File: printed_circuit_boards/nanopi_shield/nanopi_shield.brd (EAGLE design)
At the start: 48.2 x 42.9 mm, 4 parts, among them X1 1365-40

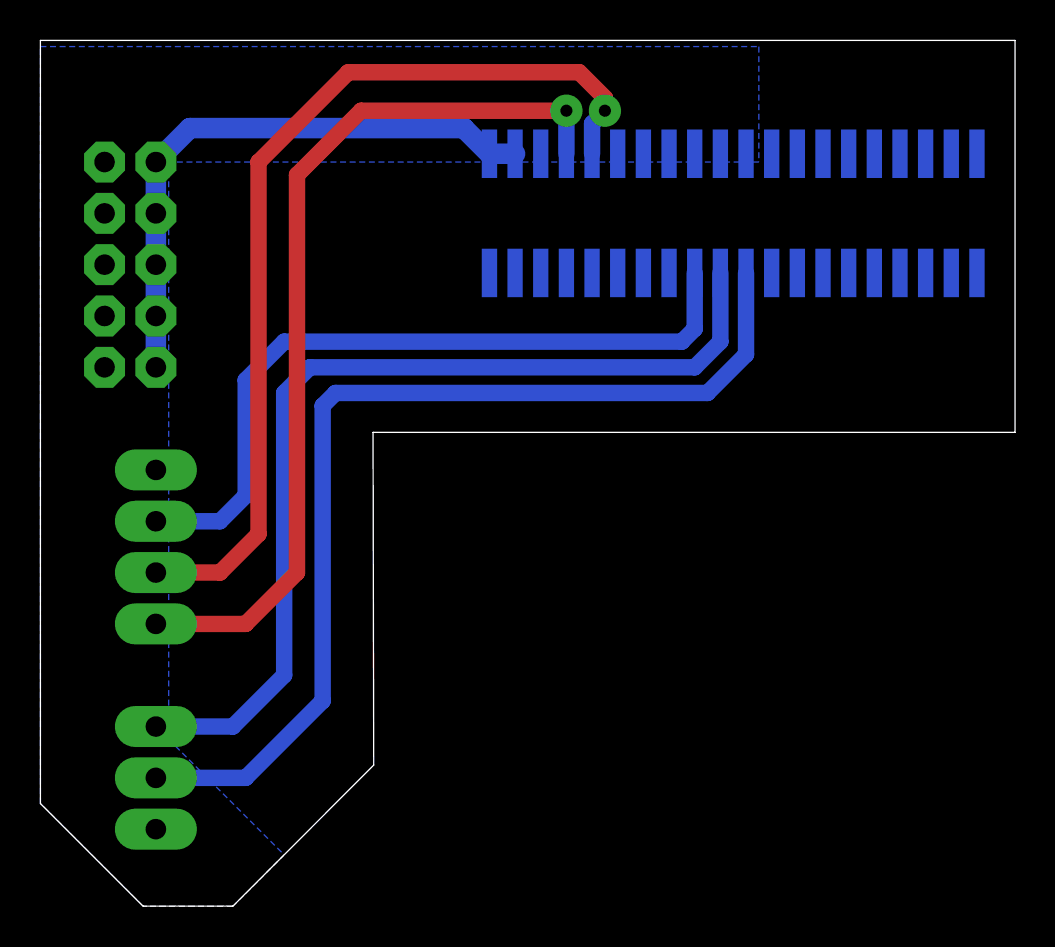
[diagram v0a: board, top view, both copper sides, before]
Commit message: Easier to solder and fix I2C
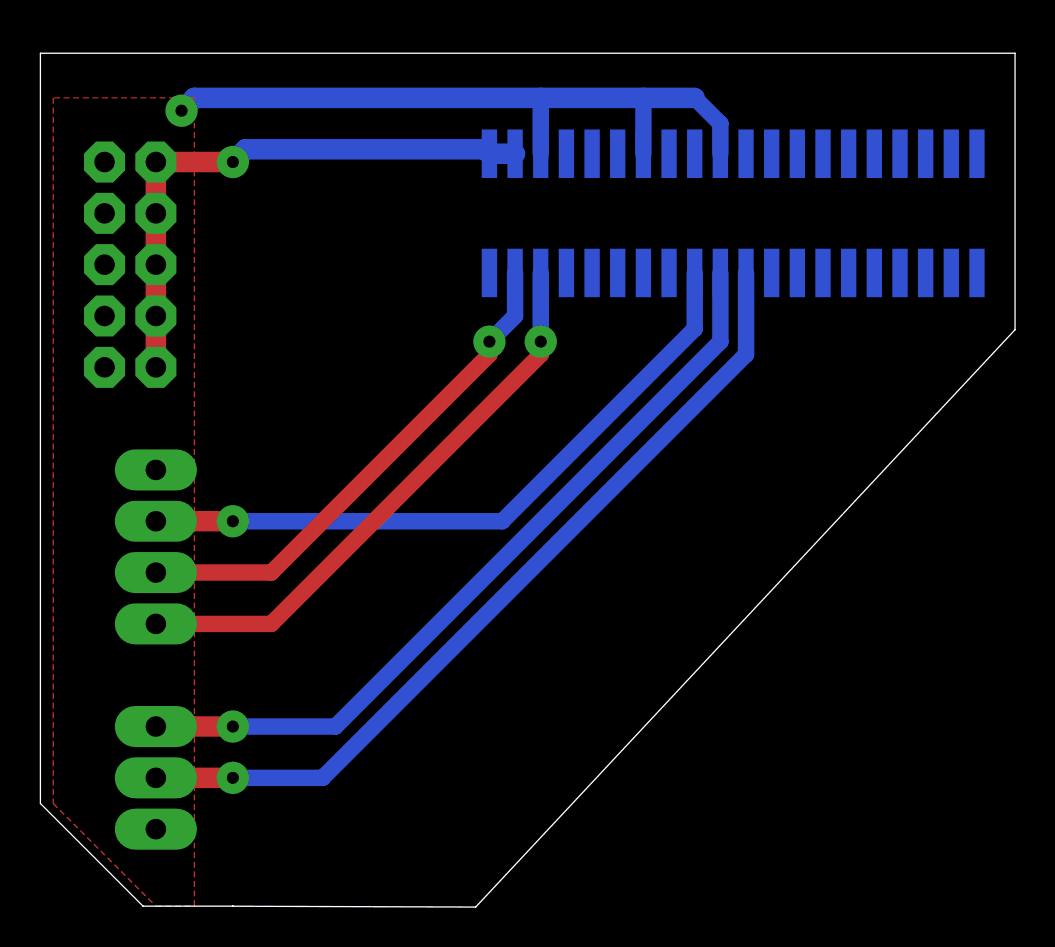
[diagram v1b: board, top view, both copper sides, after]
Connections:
- removed net I2C3_SCL: JP2.4, X1.7
- removed net I2C3_SDA: JP2.3, X1.9
- new net I2C2_SCL: JP2.4, X1.6
- new net I2C2_SDA: JP2.3, X1.4
- net N$2: now also X1.7; no longer X1.6
- net N$3: now also X1.9; no longer X1.4
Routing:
- net I2C3_SDA: track 46.8 -> 0.00 mm, vias 1 -> 0
- net I2C3_SCL: track 44.5 -> 0.00 mm, vias 1 -> 0
- net GND: track 0.00 -> 34.5 mm, vias 0 -> 1
- net I2C2_SCL: track 0.00 -> 28.6 mm, vias 0 -> 1
- net I2C2_SDA: track 0.00 -> 25.5 mm, vias 0 -> 1
- net UART_RX: track 50.5 -> 41.9 mm, vias 0 -> 1
- net UART_TX: track 47.4 -> 39.2 mm, vias 0 -> 1
- net VCC3V3_SYS: track 36.7 -> 33.4 mm, vias 0 -> 1
- net VDD_5V: track 29.2 -> 28.3 mm, vias 0 -> 1
- added copper zone on layer 1, net GND
- removed copper zone on layer 16, net GND
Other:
- board size 48.2 x 42.9 mm -> 48.2 x 42.3 mm

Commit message: MPU9250 interrupt pin
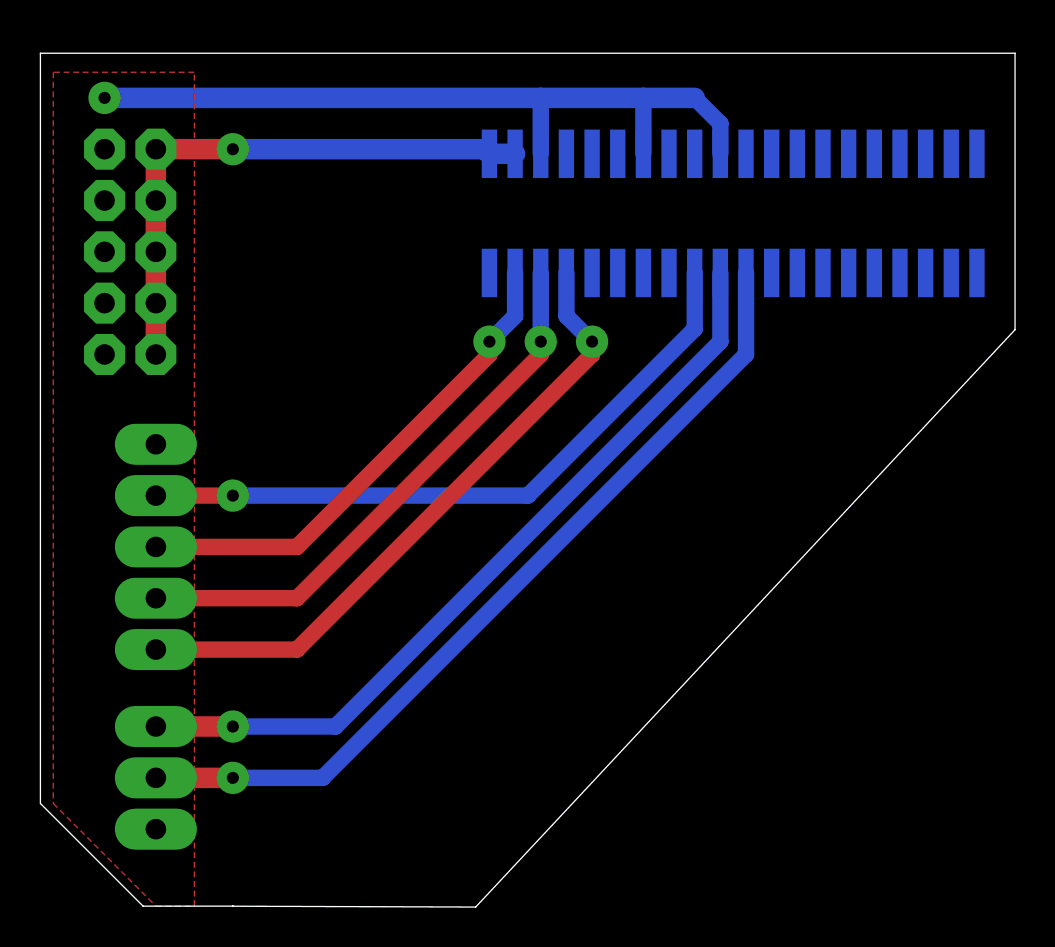
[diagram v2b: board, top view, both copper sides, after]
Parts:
- JP2: value I2C -> MPU; device pinhead:1X04 -> pinhead:1X05
- moved JP3 0.63 mm to (4.45, 32.4)
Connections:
- removed net N$1: X1.8
- new net INT: JP2.5, X1.8
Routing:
- net INT: track 0.00 -> 32.2 mm, vias 0 -> 1
- net GND: track 34.5 -> 38.0 mm
- net VCC3V3_SYS: track 33.4 -> 32.9 mm
- net I2C2_SDA: track 25.5 -> 25.0 mm
- net I2C2_SCL: track 28.6 -> 28.1 mm
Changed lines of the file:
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@@
 <drawing>
 <settings>
-<setting alwaysvectorfont="no"/>
+<setting alwaysvectorfont="yes"/>
 <setting verticaltext="up"/>
 </settings>
@@
 <attribute name="POPULARITY" value="92" x="-18.415" y="35.56" size="1.778" layer="28" rot="MR90" display="off"/>
 </element>
-<element name="JP2" library="pinhead" library_urn="urn:adsk.eagle:library:325" package="1X04" package3d_urn="urn:adsk.eagle:package:22407/2" value="I2C" x="5.715" y="17.78" smashed="yes" rot="MR270">
-<attribute name="NAME" x="3.8862" y="22.9362" size="1.27" layer="26" ratio="10" rot="MR270"/>
-<attribute name="POPULARITY" value="91" x="29.845" y="-1.27" size="1.778" layer="28" rot="MR270" display="off"/>
-</element>
-<element name="JP3" library="pinhead" library_urn="urn:adsk.eagle:library:325" package="2X05" package3d_urn="urn:adsk.eagle:package:22470/2" value="PWR" x="4.445" y="31.75" smashed="yes" rot="MR90">
-<attribute name="NAME" x="7.62" y="25.4" size="1.27" layer="26" ratio="10" rot="MR90"/>
-<attribute name="POPULARITY" value="35" x="-0.635" y="52.07" size="1.778" layer="28" rot="MR90" display="off"/>
+<element name="JP3" library="pinhead" library_urn="urn:adsk.eagle:library:325" package="2X05" package3d_urn="urn:adsk.eagle:package:22470/2" value="PWR" x="4.445" y="32.385" smashed="yes" rot="MR90">
+<attribute name="NAME" x="7.62" y="26.035" size="1.27" layer="26" ratio="10" rot="MR90"/>
+<attribute name="POPULARITY" value="35" x="-0.635" y="52.705" size="1.778" layer="28" rot="MR90" display="off"/>
 </element>
 <element name="X1" library="con-leotronics" library_urn="urn:adsk.eagle:library:160" package="1365-40" package3d_urn="urn:adsk.eagle:package:7973/1" value="1365-40" x="34.29" y="34.29" smashed="yes" rot="MR180">
@@
 <attribute name="OC_NEWARK" value="unknown" x="62.23" y="49.53" size="1.778" layer="28" rot="MR180" display="off"/>
 <attribute name="POPULARITY" value="0" x="62.23" y="49.53" size="1.778" layer="28" rot="MR180" display="off"/>
+</element>
+<element name="JP2" library="pinhead" library_urn="urn:adsk.eagle:library:325" package="1X05" package3d_urn="urn:adsk.eagle:package:22469/2" value="MPU" x="5.715" y="17.78" smashed="yes" rot="MR270">
+<attribute name="NAME" x="7.6962" y="11.5062" size="1.27" layer="26" ratio="10" rot="MR90"/>
+<attribute name="POPULARITY" value="69" x="5.715" y="17.78" size="1.778" layer="28" rot="MR270" display="off"/>
 </element>
 </elements>
@@
 <contactref element="X1" pad="1"/>
 <contactref element="X1" pad="3"/>
-<wire x1="5.715" y1="26.67" x2="5.715" y2="29.21" width="1.016" layer="1"/>
-<wire x1="5.715" y1="29.21" x2="5.715" y2="31.75" width="1.016" layer="1"/>
-<wire x1="5.715" y1="31.75" x2="5.715" y2="34.29" width="1.016" layer="1"/>
-<wire x1="5.715" y1="34.29" x2="5.715" y2="36.83" width="1.016" layer="1"/>
-<wire x1="5.715" y1="36.83" x2="9.525" y2="36.83" width="1.016" layer="1"/>
-<via x="9.525" y="36.83" extent="1-16" drill="0.6" diameter="1.6"/>
-<wire x1="22" y1="37.465" x2="10.16" y2="37.465" width="1.016" layer="16"/>
-<wire x1="9.525" y1="36.83" x2="10.16" y2="37.465" width="1.016" layer="16"/>
+<wire x1="5.715" y1="27.305" x2="5.715" y2="29.845" width="1.016" layer="1"/>
+<wire x1="5.715" y1="29.845" x2="5.715" y2="32.385" width="1.016" layer="1"/>
+<wire x1="5.715" y1="32.385" x2="5.715" y2="34.925" width="1.016" layer="1"/>
+<wire x1="5.715" y1="34.925" x2="5.715" y2="37.465" width="1.016" layer="1"/>
+<wire x1="9.525" y1="37.465" x2="5.715" y2="37.465" width="1.016" layer="1"/>
+<via x="9.525" y="37.465" extent="1-16" drill="0.6" diameter="1.6"/>
+<wire x1="22" y1="37.465" x2="9.525" y2="37.465" width="1.016" layer="16"/>
 <wire x1="22.225" y1="37.24" x2="22" y2="37.465" width="1.016" layer="16"/>
 <wire x1="22.225" y1="37.24" x2="23.495" y2="37.24" width="1.016" layer="16"/>
@@
 <contactref element="JP3" pad="9"/>
 <contactref element="JP1" pad="1"/>
-<contactref element="JP2" pad="1"/>
 <contactref element="X1" pad="5"/>
 <contactref element="X1" pad="13"/>
 <contactref element="X1" pad="19"/>
 <polygon width="1.016" layer="1" isolate="0.8128" thermals="no">
-<vertex x="0.635" y="40.005"/>
+<vertex x="0.635" y="41.275"/>
 <vertex x="0.635" y="5.08"/>
 <vertex x="5.715" y="0"/>
 <vertex x="7.62" y="0"/>
-<vertex x="7.62" y="40.005"/>
+<vertex x="7.62" y="41.275"/>
 </polygon>
-<via x="6.985" y="39.37" extent="1-16" drill="0.6" diameter="1.6"/>
-<wire x1="6.985" y1="39.37" x2="7.62" y2="40.005" width="1.016" layer="16"/>
-<wire x1="7.62" y1="40.005" x2="24.765" y2="40.005" width="1.016" layer="16"/>
+<via x="3.175" y="40.005" extent="1-16" drill="0.6" diameter="1.6"/>
+<wire x1="3.175" y1="40.005" x2="24.765" y2="40.005" width="1.016" layer="16"/>
 <wire x1="24.765" y1="40.005" x2="24.765" y2="37.24" width="0.8128" layer="16"/>
 <wire x1="24.765" y1="40.005" x2="29.845" y2="40.005" width="1.016" layer="16"/>
@@
 <wire x1="32.385" y1="40.005" x2="33.655" y2="38.735" width="0.8128" layer="16"/>
 <wire x1="33.655" y1="38.735" x2="33.655" y2="37.24" width="0.8128" layer="16"/>
+<contactref element="JP2" pad="1"/>
 </signal>
 <signal name="N$23">
@@
 </signal>
 <signal name="VCC3V3_SYS">
-<contactref element="JP2" pad="2"/>
 <contactref element="X1" pad="18"/>
 <wire x1="32.385" y1="31.34" x2="32.385" y2="28.575" width="0.8128" layer="16"/>
-<wire x1="32.385" y1="28.575" x2="22.86" y2="19.05" width="0.8128" layer="16"/>
-<wire x1="22.86" y1="19.05" x2="9.525" y2="19.05" width="0.8128" layer="16"/>
-<via x="9.525" y="19.05" extent="1-16" drill="0.6" diameter="1.6"/>
-<wire x1="5.715" y1="19.05" x2="9.525" y2="19.05" width="1.016" layer="1"/>
+<wire x1="32.385" y1="28.575" x2="24.13" y2="20.32" width="0.8128" layer="16"/>
+<wire x1="24.13" y1="20.32" x2="9.525" y2="20.32" width="0.8128" layer="16"/>
+<via x="9.525" y="20.32" extent="1-16" drill="0.6" diameter="1.6"/>
+<contactref element="JP2" pad="2"/>
+<wire x1="9.525" y1="20.32" x2="5.715" y2="20.32" width="0.8128" layer="1"/>
 </signal>
 <signal name="UART_TX">
@@
 <contactref element="X1" pad="39"/>
 </signal>
-<signal name="N$1">
-<contactref element="X1" pad="8"/>
-</signal>
 <signal name="I2C2_SCL">
 <contactref element="X1" pad="6"/>
+<wire x1="24.765" y1="27.94" x2="24.765" y2="27.305" width="0.8128" layer="1"/>
+<wire x1="24.765" y1="27.305" x2="12.7" y2="15.24" width="0.8128" layer="1"/>
+<via x="24.765" y="27.94" extent="1-16" drill="0.6" diameter="1.6"/>
+<wire x1="24.765" y1="27.94" x2="24.765" y2="31.34" width="0.8128" layer="16"/>
 <contactref element="JP2" pad="4"/>
-<wire x1="24.765" y1="27.94" x2="24.765" y2="27.305" width="0.8128" layer="1"/>
-<wire x1="24.765" y1="27.305" x2="11.43" y2="13.97" width="0.8128" layer="1"/>
-<via x="24.765" y="27.94" extent="1-16" drill="0.6" diameter="1.6"/>
-<wire x1="11.43" y1="13.97" x2="5.715" y2="13.97" width="0.8128" layer="1"/>
-<wire x1="24.765" y1="27.94" x2="24.765" y2="31.34" width="0.8128" layer="16"/>
+<wire x1="12.7" y1="15.24" x2="5.715" y2="15.24" width="0.8128" layer="1"/>
 </signal>
 <signal name="I2C2_SDA">
 <contactref element="X1" pad="4"/>
-<contactref element="JP2" pad="3"/>
 <wire x1="22.225" y1="27.94" x2="22.225" y2="27.305" width="0.8128" layer="1"/>
-<wire x1="22.225" y1="27.305" x2="11.43" y2="16.51" width="0.8128" layer="1"/>
+<wire x1="22.225" y1="27.305" x2="12.7" y2="17.78" width="0.8128" layer="1"/>
 <via x="22.225" y="27.94" extent="1-16" drill="0.6" diameter="1.6"/>
-<wire x1="11.43" y1="16.51" x2="5.715" y2="16.51" width="0.8128" layer="1"/>
 <wire x1="22.225" y1="27.94" x2="23.495" y2="29.21" width="0.8128" layer="16"/>
 <wire x1="23.495" y1="29.21" x2="23.495" y2="31.34" width="0.8128" layer="16"/>
+<contactref element="JP2" pad="3"/>
+<wire x1="12.7" y1="17.78" x2="5.715" y2="17.78" width="0.8128" layer="1"/>
 </signal>
 <signal name="N$4">
@@
 <contactref element="X1" pad="9"/>
 </signal>
+<signal name="INT">
+<contactref element="JP2" pad="5"/>
+<contactref element="X1" pad="8"/>
+<wire x1="26.035" y1="31.34" x2="26.035" y2="29.21" width="0.8128" layer="16"/>
+<wire x1="26.035" y1="29.21" x2="27.305" y2="27.94" width="0.8128" layer="16"/>
+<via x="27.305" y="27.94" extent="1-16" drill="0.6" diameter="1.6"/>
+<wire x1="27.305" y1="27.94" x2="27.305" y2="27.305" width="0.8128" layer="1"/>
+<wire x1="27.305" y1="27.305" x2="12.7" y2="12.7" width="0.8128" layer="1"/>
+<wire x1="12.7" y1="12.7" x2="5.715" y2="12.7" width="0.8128" layer="1"/>
+</signal>
 </signals>
